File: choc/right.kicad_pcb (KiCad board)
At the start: 2 copper layers, 117 x 92 mm, 87 parts, among them J2 USB_B_Micro, SW24 SW_Push, SW25 SW_Push, SW26 SW_Push, SW27 SW_Push, SW28 SW_Push, SW29 SW_Push, SW30 SW_Push, SW31 SW_Push, SW32 SW_Push, SW33 SW_Push, SW34 SW_Push, SW35 SW_Push, SW36 SW_Push, SW37 SW_Push, SW38 SW_Push, SW39 SW_Push, SW40 SW_Push, SW41 SW_Push, SW42 SW_Push, SW43 SW_Push, SW44 SW_Push, SW45 SW_Push, SW46 SW_Push, SW48 SW_Push, SW50 SW_Push, U2 ProMicro

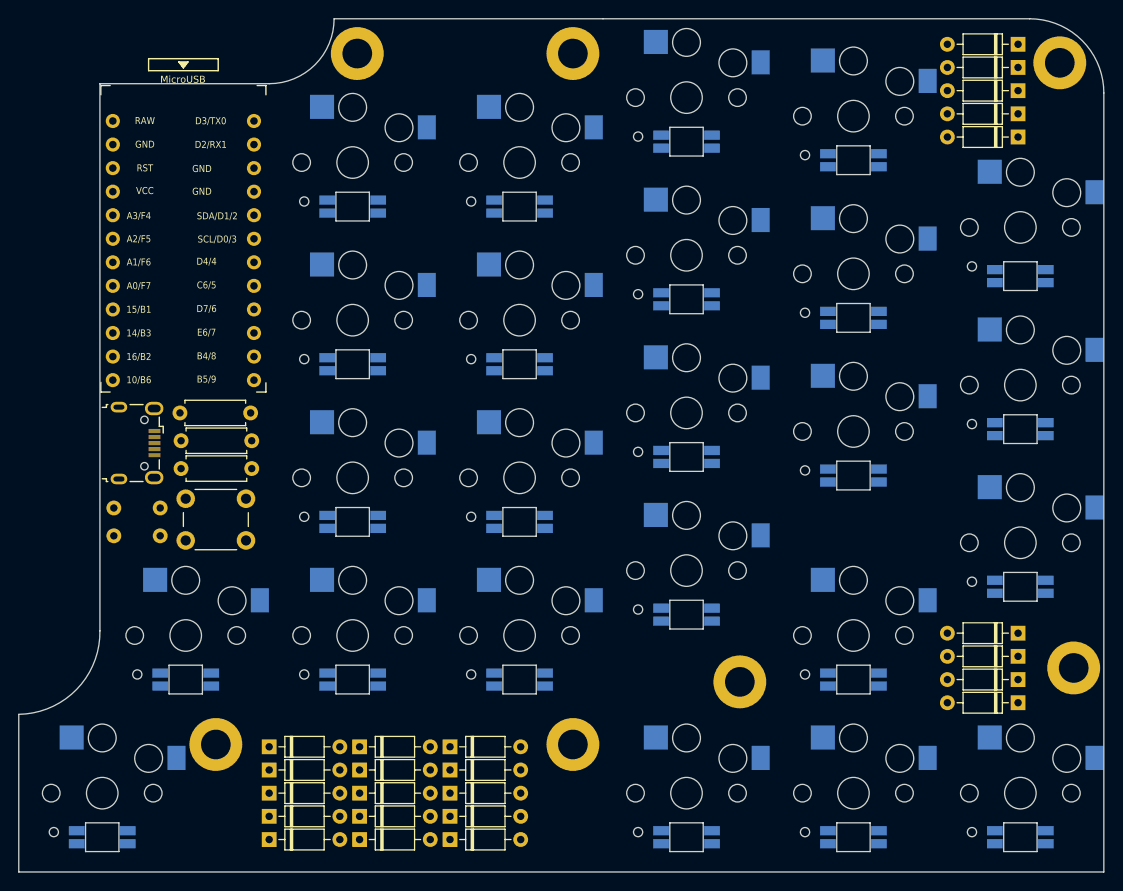
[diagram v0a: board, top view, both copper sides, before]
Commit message: add routed right board
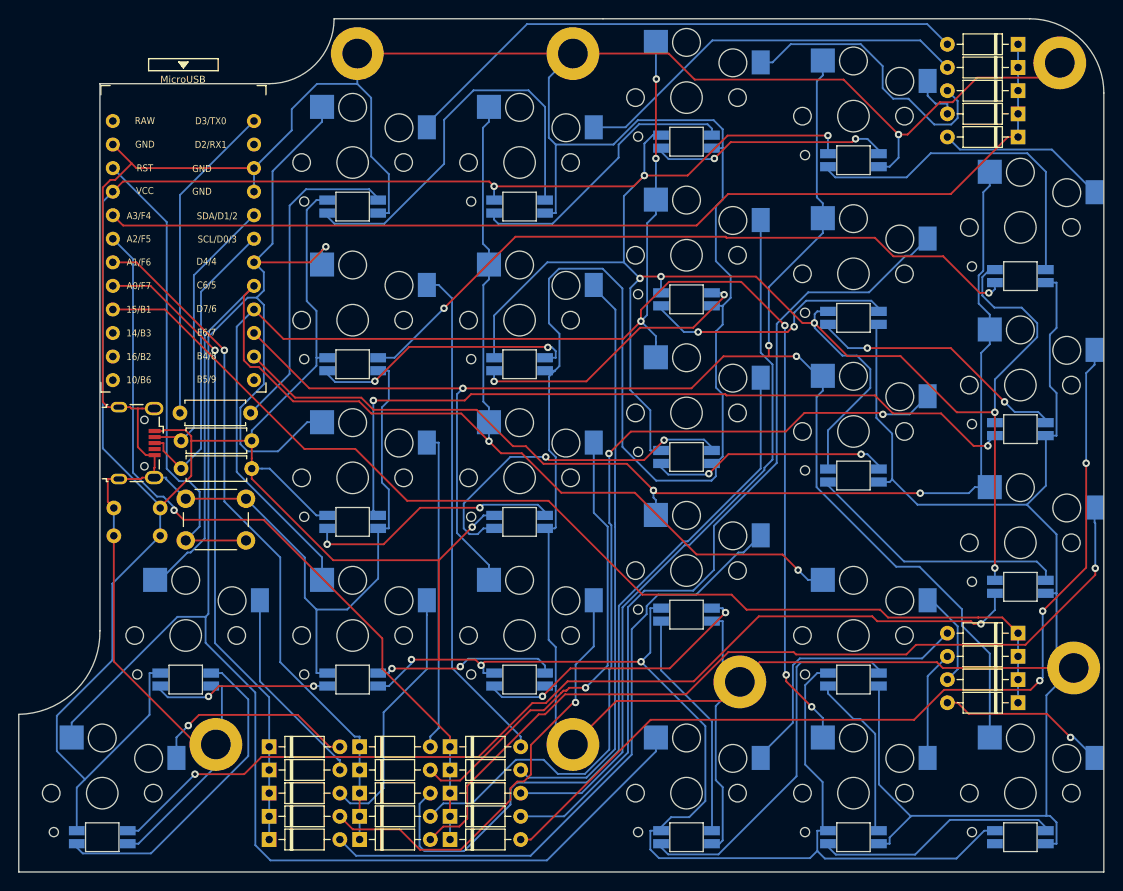
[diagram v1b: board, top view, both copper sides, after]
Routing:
- net GND: track 0.00 -> 716.7 mm, vias 0 -> 1
- net +5V: track 0.00 -> 586.8 mm, vias 0 -> 12
- net /rcol0: track 0.00 -> 197.7 mm, vias 0 -> 1
- net /rcol2: track 0.00 -> 179.0 mm, vias 0 -> 6
- net /rcol3: track 0.00 -> 172.0 mm, vias 0 -> 3
- net /rcol1: track 0.00 -> 154.4 mm, vias 0 -> 2
- net /rcol4: track 0.00 -> 123.9 mm, vias 0 -> 2
- net /rrow4: track 0.00 -> 119.6 mm
- net /rrow0: track 0.00 -> 112.0 mm
- net Net-(LED27-Pad4): track 0.00 -> 105.8 mm, vias 0 -> 2
- net Net-(D44-Pad2): track 0.00 -> 101.2 mm, vias 0 -> 3
- net Net-(D45-Pad2): track 0.00 -> 93.1 mm, vias 0 -> 1
- net Net-(D41-Pad2): track 0.00 -> 92.7 mm, vias 0 -> 2
- net Net-(D40-Pad2): track 0.00 -> 90.5 mm
- net /rrow1: track 0.00 -> 85.3 mm, vias 0 -> 1
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
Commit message: remove leds from choc
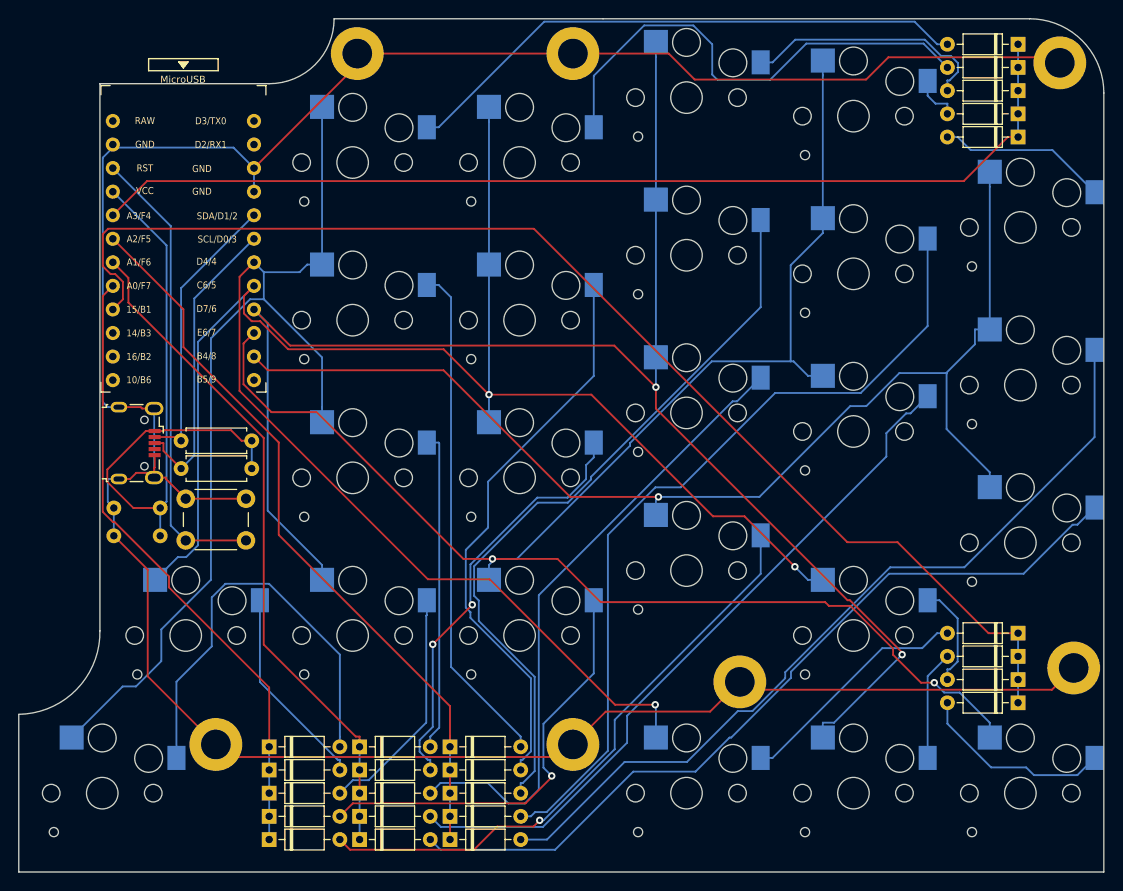
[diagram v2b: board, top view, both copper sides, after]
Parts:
- removed LED24, LED25, LED26, LED27, LED28, LED29, LED30, LED31, LED32, LED33, LED34, LED35, LED36, LED37, LED38, LED39, LED40, LED41, LED42, LED43, LED44, LED45, LED46, LED48: YS-SK6812MINI-E, kbd:YS-SK6812MINI-E
- removed R6: 1k, Resistor_THT:R_Axial_DIN0207_L6.3mm_D2.5mm_P7.62mm_Horizontal
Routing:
- net +5V: track 586.8 -> 68.8 mm, vias 12 -> 0
- net GND: track 716.7 -> 305.1 mm, vias 1 -> 0
- net Net-(LED27-Pad4): track 105.8 -> 0.00 mm, vias 2 -> 0
- net Net-(LED26-Pad4): track 82.9 -> 0.00 mm, vias 2 -> 0
- net Net-(LED25-Pad4): track 75.3 -> 0.00 mm, vias 2 -> 0
- net Net-(LED24-Pad2): track 43.7 -> 0.00 mm
- net Net-(LED28-Pad2): track 40.4 -> 0.00 mm
- net Net-(LED31-Pad2): track 37.1 -> 0.00 mm, vias 2 -> 0
- net Net-(LED39-Pad2): track 36.6 -> 0.00 mm
- net Net-(LED24-Pad4): track 35.0 -> 0.00 mm
- net Net-(LED27-Pad2): track 34.8 -> 0.00 mm
- net /rLED: track 34.8 -> 0.00 mm
- net Net-(LED30-Pad2): track 31.4 -> 0.00 mm, vias 2 -> 0
- net Net-(LED42-Pad2): track 31.2 -> 0.00 mm, vias 2 -> 0
- net Net-(LED29-Pad2): track 30.6 -> 0.00 mm
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
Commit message: add buzzer to pcb
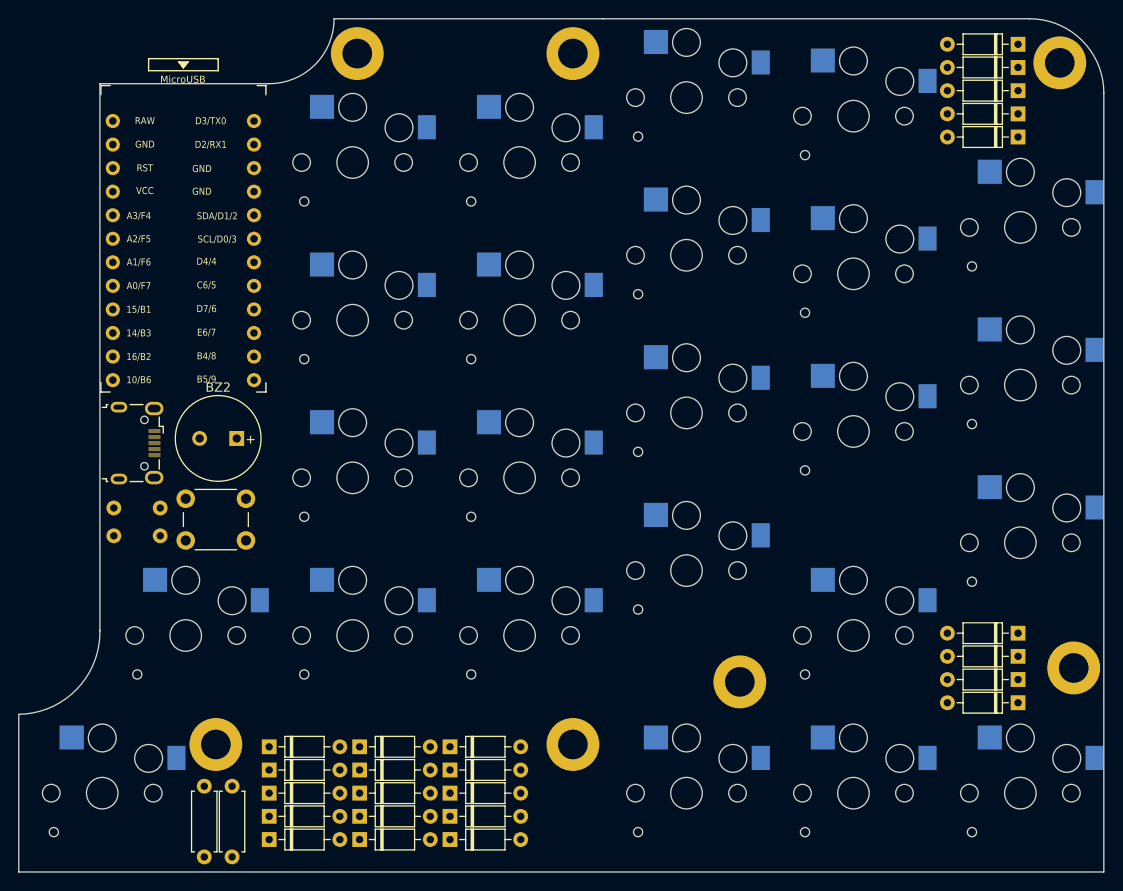
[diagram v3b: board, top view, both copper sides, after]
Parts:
- added BZ2: Buzzer, Buzzer_Beeper:MagneticBuzzer_PUI_AT-0927-TT-6-R, F.Cu at (181.5, 63.0)
- moved R4 37.7 mm to (181.0, 100.5), turned to -90 degrees
- moved R3 34.3 mm to (178.0, 100.5), turned to -90 degrees
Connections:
- U2 pad 12: unconnected-(U2-Pad12) -> /rbuzzer
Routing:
- net GND: track 305.1 -> 0.00 mm
- net /rcol3: track 185.1 -> 0.00 mm, vias 2 -> 0
- net /rcol0: track 178.4 -> 0.00 mm, vias 1 -> 0
- net /rcol2: track 169.4 -> 0.00 mm, vias 2 -> 0
- net /rcol1: track 148.4 -> 0.00 mm, vias 2 -> 0
- net /rrow4: track 134.3 -> 0.00 mm
- net /rcol4: track 127.3 -> 0.00 mm, vias 1 -> 0
- net /rrow0: track 111.1 -> 0.00 mm
- net Net-(D44-Pad2): track 89.6 -> 0.00 mm
- net Net-(D40-Pad2): track 88.9 -> 0.00 mm
- net Net-(D45-Pad2): track 87.8 -> 0.00 mm
- net Net-(D35-Pad2): track 80.0 -> 0.00 mm
- net /rrow1: track 79.8 -> 0.00 mm
- net Net-(D41-Pad2): track 76.5 -> 0.00 mm
- net /rrow2: track 73.5 -> 0.00 mm
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
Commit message: import right ses
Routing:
- net GND: track 0.00 -> 309.4 mm
- net /rcol2: track 0.00 -> 175.0 mm, vias 0 -> 2
- net /rcol3: track 0.00 -> 169.2 mm, vias 0 -> 3
- net /rcol0: track 0.00 -> 167.4 mm
- net /rcol1: track 0.00 -> 149.9 mm, vias 0 -> 2
- net /rrow4: track 0.00 -> 130.0 mm
- net /rcol4: track 0.00 -> 122.0 mm, vias 0 -> 1
- net /rrow0: track 0.00 -> 111.1 mm
- net /rrow1: track 0.00 -> 111.0 mm
- net Net-(D44-Pad2): track 0.00 -> 108.2 mm
- net /rSDA: track 0.00 -> 98.0 mm
- net Net-(D45-Pad2): track 0.00 -> 91.8 mm, vias 0 -> 1
- net +5V: track 0.00 -> 89.7 mm
- net Net-(D40-Pad2): track 0.00 -> 88.5 mm
- net Net-(D41-Pad2): track 0.00 -> 86.5 mm
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
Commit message: fix right
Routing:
- net /rSDA: track 98.0 -> 99.3 mm
- net GND: track 309.4 -> 310.3 mm
- net Net-(D36-Pad2): track 67.1 -> 67.6 mm
- net /rrow3: track 79.6 -> 80.1 mm
